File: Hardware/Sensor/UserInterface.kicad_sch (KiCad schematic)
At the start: 24 parts, among them Q5 Q_NPN_BEC, Q8 Q_PMOS_GDS, Q9 Q_NMOS_GDS, SW1 UP, SW2 DOWN, SW3 LEFT, SW4 RIGHT, U1 SSD1306

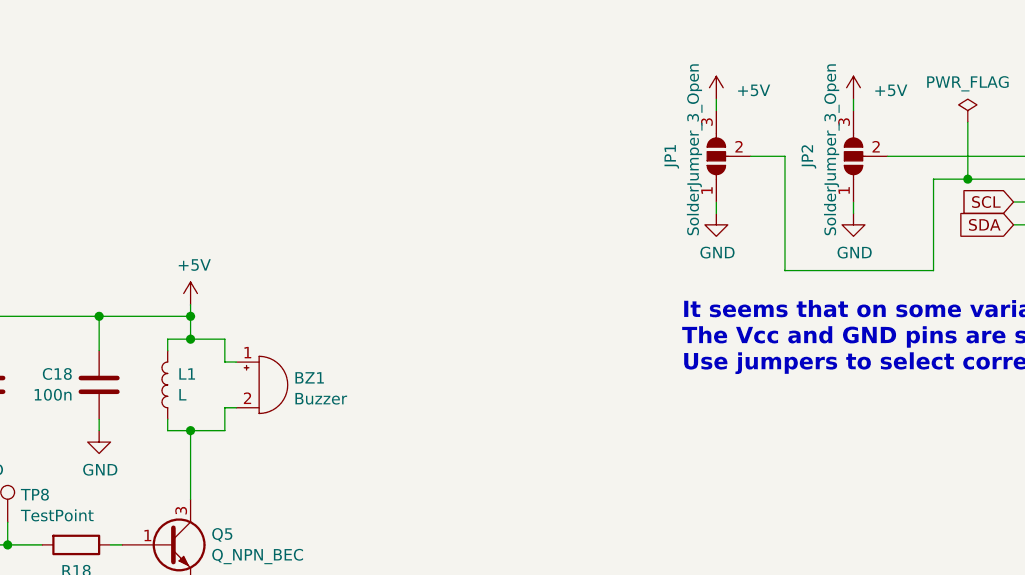
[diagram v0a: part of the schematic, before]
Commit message: this is what was send for pcb production
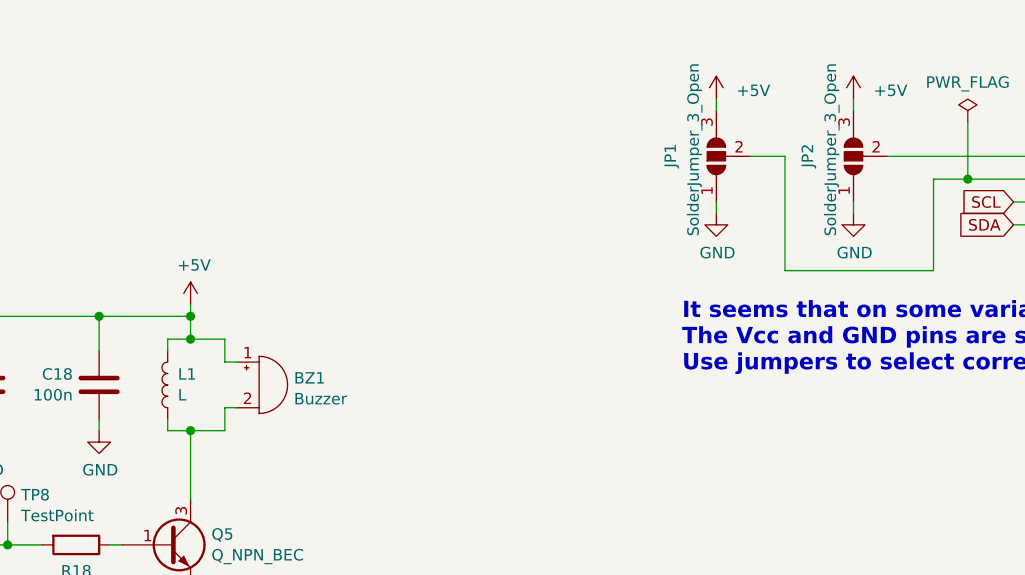
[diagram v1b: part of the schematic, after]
